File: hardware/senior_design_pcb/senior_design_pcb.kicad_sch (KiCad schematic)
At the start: 72 parts, among them J1 SBH11-PBPC-D05-ST-BK, J10 Conn_01x04_Socket, J11 2x08Rectangle-LED Matrix Conn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, J12 1x05JST - Joystick2 connector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, J13 UJ20-C-H-C-4-SMT-TR, J2 Conn_01x08_Pin, J3 Conn_01x02_Socket, J4 Conn_01x02_Socket, J5 1x05JST-Admin LCD Console Con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, J6 1x05JST - Joystick1 connector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, J9 Conn_01x04_Socket, SW3 1x02JST-Admin Console button 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, U1 USBLC6-2SC6Y, U2 STM32F091RCTx, U3 LD1117S33TR_SOT223, U4 KMR241GLFS, U5 USBLC6-2SC6Y, U6 2SA1873-GRTE85L_F, U7 2SA1873-GRTE85L_F, U8 2SA1873-GRTE85L_F

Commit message: routed more traces
just routed some more. oh and i also added an LED bc there was a pin i forgot we werent using anymore so like why not make it an on board led yk.
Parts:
- removed U1: USBLC6-2SC6Y, kicad_library:TVS-DIODE-USBLC6-2SC6Y, symbol TVS-DIODE-USBLC6-2SC6Y:USBLC6-2SC6Y
- added C27, C28, C29: .1uF, Capacitor_SMD:C_0805_2012Metric_Pad1.18x1.45mm_HandSolder, symbol Device:C
- added H1, H2, H3, H4: MountingHole, MountingHole:MountingHole_3.2mm_M3, symbol Mechanical:MountingHole
- added LD3, LD4: LED_Red, LED_SMD:LED_0805_2012Metric, symbol Device:LED_Small_ALT
- added LD5: LED_Yel, LED_SMD:LED_0805_2012Metric, symbol Device:LED_Small_ALT
- added R14: 5k11, Resistor_SMD:R_0805_2012Metric_Pad1.20x1.40mm_HandSolder, symbol Device:R_US
- added R16, R18, R19: 10K, Resistor_SMD:R_0805_2012Metric_Pad1.20x1.40mm_HandSolder, symbol Device:R_US
- added R20, R21: 68, Resistor_SMD:R_0805_2012Metric_Pad1.20x1.40mm_HandSolder, symbol Device:R_US
- added U1, U10, U9: KMR241GLFS, General Library:KMR241G-RESET-BUTTON, symbol KMR241G-RESET-BUTTON:KMR241GLFS
- C14, C16: value 4.7uf -> 4.7uF
- R11, R13, R15: footprint (none) -> Resistor_SMD:R_0805_2012Metric_Pad1.20x1.40mm_HandSolder
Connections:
- net IR_IN_1-dir is gone; now on net GND: J3.1 (Pin_1)
- net IR_IN_2-dir is gone; now on net GND: J4.1 (Pin_1)
- net +3V3: now also J2.1 (Pin_1), J5.5 (Pin_5), J6.5 (Pin_5), R16.1, R18.1, R19.1; no longer J5.1 (Pin_1), J6.1 (Pin_1)
- net ADMIN_JOYSTICK-BUTTON: now also J6.4 (Pin_4); no longer J6.2 (Pin_2)
- net ADMIN_JOYSTICK-Y: now also J6.2 (Pin_2); no longer J6.4 (Pin_4)
- net CONSOLE_DISP-1: now also J5.4 (Pin_4); no longer J5.2 (Pin_2)
- net CONSOLE_DISP-3: now also J5.2 (Pin_2); no longer J5.4 (Pin_4)
- net DIR+1: now also J9.3 (Pin_3); no longer J9.2 (Pin_2)
- net DIR+2: now also J10.3 (Pin_3); no longer J10.2 (Pin_2)
- net ENA+1: now also J9.2 (Pin_2); no longer J9.3 (Pin_3)
- net ENA+2: now also J10.2 (Pin_2); no longer J10.3 (Pin_3)
- net GND: now also J10.1 (Pin_1), J2.8 (Pin_8), J5.1 (Pin_1), J6.1 (Pin_1), J9.1 (Pin_1), C27.2, C28.2, C29.2, LD3.1 (K), LD4.1 (K), LD5.1 (K), U1.2, U1.3, U10.2, U10.3, U9.2, U9.3; no longer J10.4 (Pin_4), J3.2 (Pin_2), J4.2 (Pin_2), J5.5 (Pin_5), J6.5 (Pin_5), J9.4 (Pin_4)
- net IR_IN_1: now also J3.2 (Pin_2)
- net IR_IN_2: now also J4.2 (Pin_2)
- net PA0: now also C27.1, R16.2, U1.1, U1.4
- net PA1: now also C28.1, R18.2, U9.1, U9.4
- net PB15: now also R20.1
- net PB2: now also C29.1, R19.2, U10.1, U10.4
- net PB3: now also J2.2 (Pin_2)
- net PB5: now also J2.3 (Pin_3)
- net PB6: now also J2.4 (Pin_4)
- net PB7: now also J2.5 (Pin_5)
- net PB8: now also J2.6 (Pin_6)
- net PB9: now also J2.7 (Pin_7)
- net PC3: now also R21.1
- net PUL+1: now also J9.4 (Pin_4); no longer J9.1 (Pin_1)
- net PUL+2: now also J10.4 (Pin_4); no longer J10.1 (Pin_1)
- net VBUS: now also R14.2
- new net: LD3.2 (A), R14.1
- new net: LD4.2 (A), R20.2
- new net: LD5.2 (A), R21.2
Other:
- note added: "On board buttons"
- note removed: "Reset button"
- moved on the sheet: J10, J11, J2, J9, R11, R13, R15, U6, U7, U8

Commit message: cleaned up
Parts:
- removed TP1: TestPoint_Small, TestPoint:TestPoint_Pad_D1.5mm, symbol Connector:TestPoint_Small
- C20, C21: value 12.5pF -> 15pF
- FT1: value ~ -> FT232
- J1: footprint General Library:jtag_conn -> Sr_ Design:jtag_conn
- U1, U10, U4, U9: footprint General Library:KMR241G-RESET-BUTTON -> kicad_library:KMR241G-RESET-BUTTON
- U5: footprint kicad_library:TVS-DIODE-USBLC6-2SC6Y -> Sr_ Design:TVS-DIODE-USBLC6-2SC6Y
- XTAL2: value 8MHz(8PF) -> 8MHz(15pF)
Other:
- note added: "mounting holes"
- note removed: "600 Ohm @ 100MHz .3 Ohm DCR, 500 mA"
- note removed: "BOOT0 PDR"
- note removed: "Communications"
- note removed: "one for each pin connected to VDD, 4.7uF bulk caps near source"
- note removed: "should we have a clock select jumper like the 362 board?"
- note removed: "two diff kinds of tp - pad (left) and drill hole (right):"
- moved on the sheet: C1, C10, C11, C12, C13, C14, C15, C16, C17, C18, C19, C2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

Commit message: reorganized
updated + finished reorg
added footprints
added 2x8 jtag 3d file
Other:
- moved on the sheet: J12

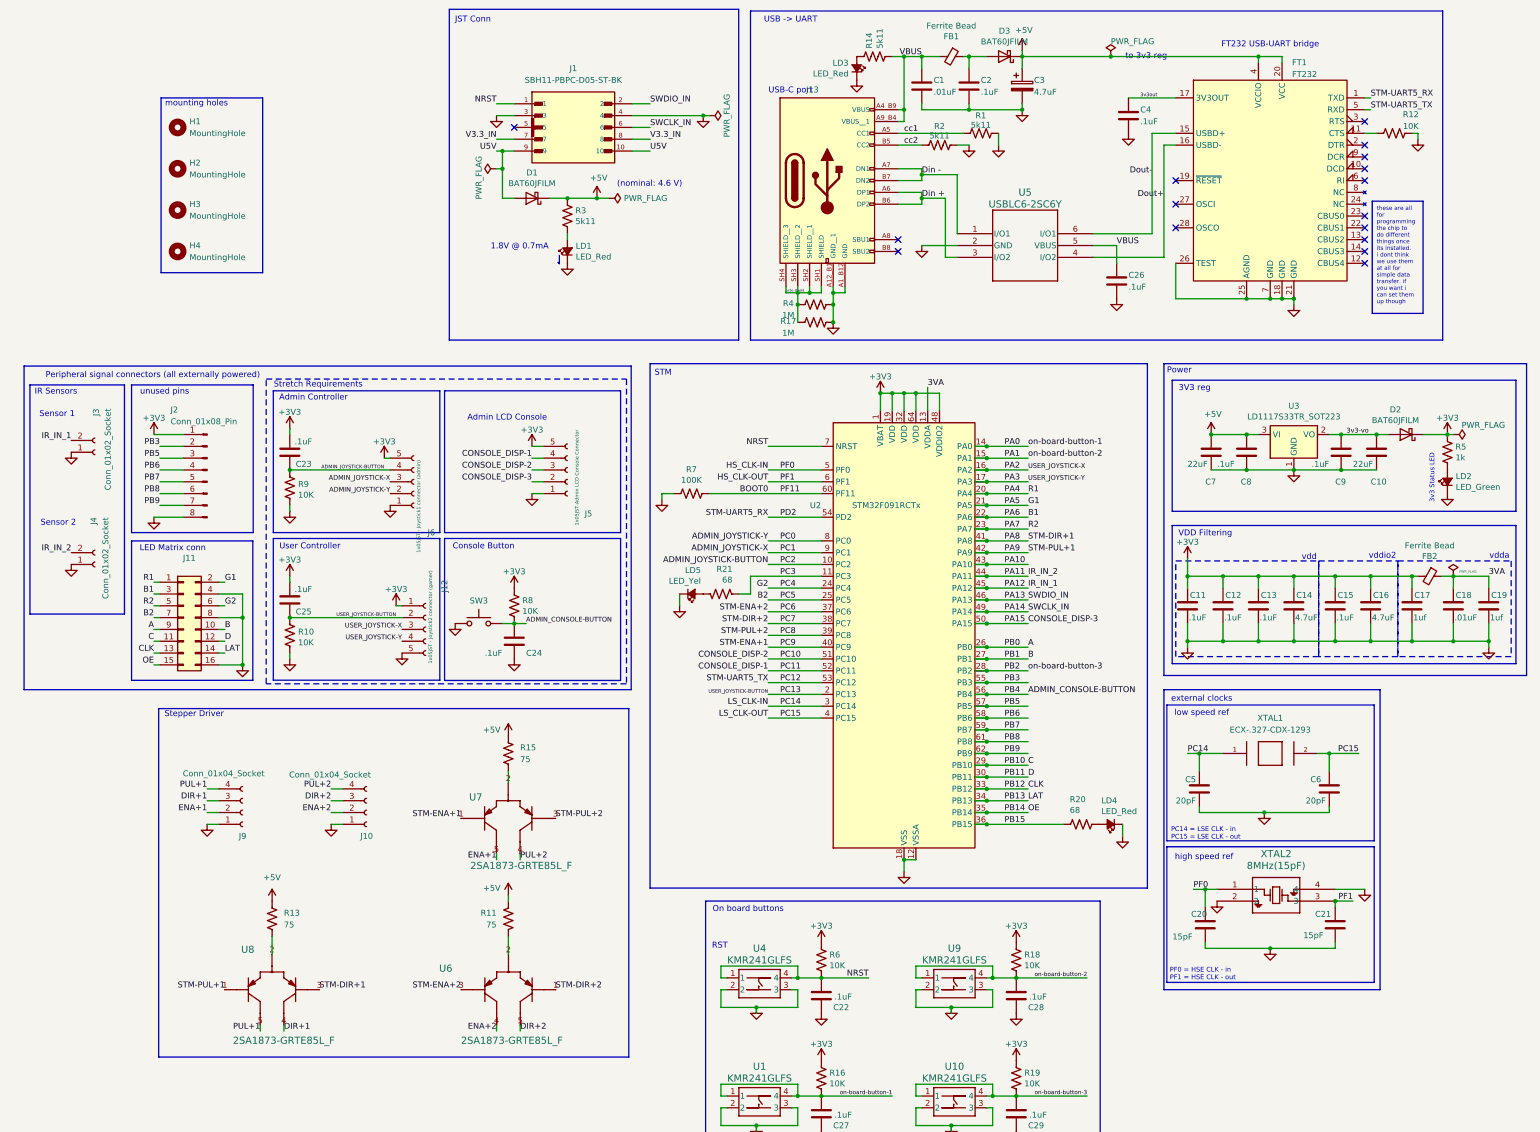
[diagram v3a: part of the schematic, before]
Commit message: 3v3 exclusion zones
decoupling caps had connection to 3v3 straight to the pin. should route through the cap not just be attached. adding exclusion zones to vias and routing 3v3 to the cap pad
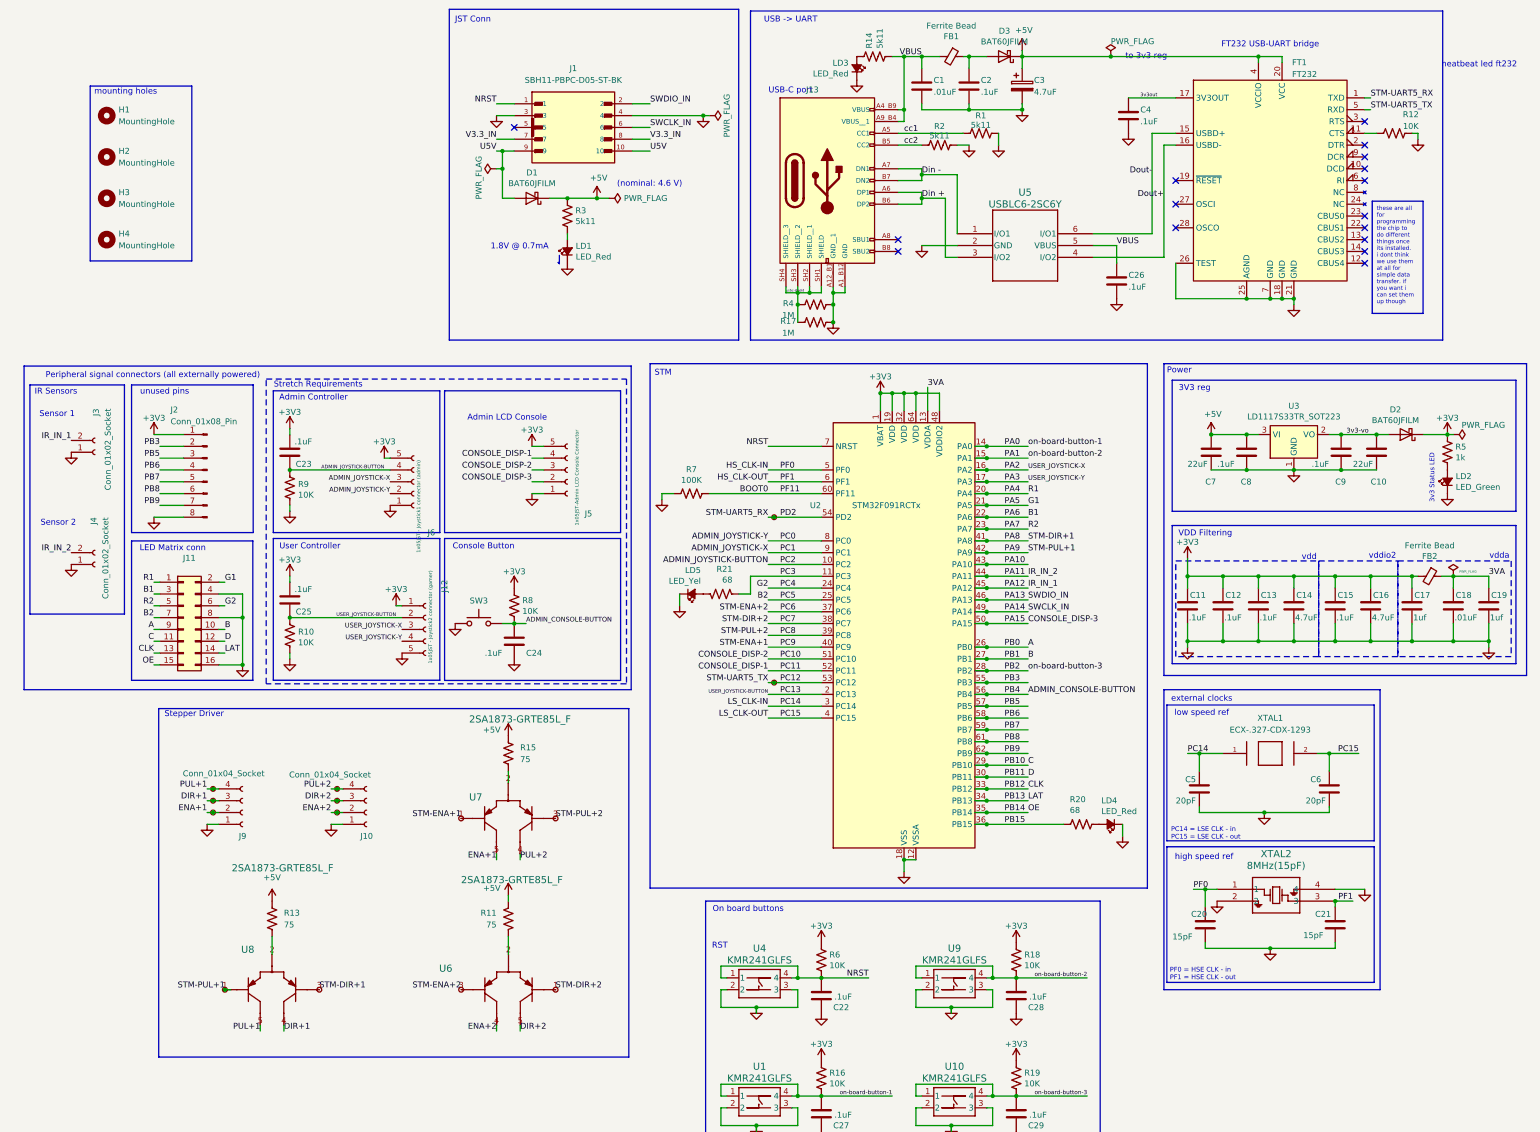
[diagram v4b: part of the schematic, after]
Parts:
- added TP1, TP13, TP14, TP2, TP3, TP4, TP5, TP6: TestPoint_Small, TestPoint:TestPoint_THTPad_D1.0mm_Drill0.5mm, symbol testpoint:TestPoint_Small
- added TP10, TP11, TP12, TP7, TP8, TP9: TestPoint_Small, symbol testpoint:TestPoint_Small
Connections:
- net DIR+1: now also TP5.1
- net DIR+2: now also TP2.1
- net ENA+1: now also TP6.1
- net ENA+2: now also TP3.1
- net PA8: now also TP12.1
- net PA9: now also TP11.1
- net PC12: now also TP13.1
- net PC6: now also TP7.1
- net PC7: now also TP8.1
- net PC8: now also TP10.1
- net PC9: now also TP9.1
- net PD2: now also TP14.1
- net PUL+1: now also TP4.1
- net PUL+2: now also TP1.1
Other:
- note added: "heatbeat led ft232"
- moved on the sheet: H1, H2, H3, H4
